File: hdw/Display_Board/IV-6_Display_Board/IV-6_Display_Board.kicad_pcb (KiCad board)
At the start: 4 copper layers, 200 x 50 mm, 236 parts, among them J3001 DSP_IO_Connector, Q1101 PMSTA06, Q1102 BC856W, Q1103 PMSTA06, Q1104 BC856W, Q1105 PMSTA06, Q1106 BC856W, Q1107 PMSTA06, Q1108 BC856W, Q201 PMSTA06, Q202 PMSTA06, Q203 BC856W, Q204 BC856W, Q205 PMSTA06, Q206 PMSTA06, Q207 BC856W, Q208 BC856W, Q209 PMSTA06, Q210 PMSTA06, Q211 BC856W, Q212 BC856W, Q213 PMSTA06, Q214 PMSTA06, Q215 BC856W, Q216 BC856W, Q301 PMSTA06, Q302 PMSTA06, Q303 BC856W, Q304 BC856W, Q305 PMSTA06, Q306 PMSTA06, Q307 BC856W, Q308 BC856W, Q309 PMSTA06, Q310 PMSTA06, Q311 BC856W, Q312 BC856W, SW601 Cap_Touch, SW602 Cap_Touch, SW801 Cap_Touch, SW802 Cap_Touch, SW901 Cap_Touch, U1001 MCP9804, U1301 DS1683, U1302 LTC4316DD, U501 TCA9555RGER, U601 TLV71333PDBV, U602 TLV71333PDBV, U603 AT42QT1010-TSHR, U604 AT42QT1010-TSHR, U605 74LVC1G97, U606 74LVC1G97, U801 TLV71333PDBV, U802 TLV71333PDBV, U803 AT42QT1010-TSHR, U804 AT42QT1010-TSHR, U805 74LVC1G97, U806 74LVC1G97, U901 TLV71333PDBV, U902 AT42QT1010-TSHR, U903 74LVC1G97

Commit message: rotated VFDs
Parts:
- moved Q310 158.3 mm to (368.8, 49.6)
- moved R318 158.3 mm to (368.8, 52.2)
- moved Q301 158.3 mm to (213.2, 49.6)
- moved Q303 158.3 mm to (213.2, 45.0)
- moved Q305 158.3 mm to (235.5, 49.6)
- moved Q306 158.3 mm to (346.6, 49.6)
- moved Q307 158.3 mm to (235.5, 45.0)
- moved Q308 158.3 mm to (346.6, 45.0)
- moved Q309 158.3 mm to (279.9, 49.6)
- moved Q311 158.3 mm to (279.9, 45.0)
- moved Q312 158.3 mm to (368.8, 45.0)
- moved R301 158.3 mm to (213.2, 52.2)
- moved R303 158.3 mm to (216.0, 45.1)
- moved R304 158.3 mm to (213.2, 47.1)
- moved R305 158.3 mm to (304.9, 45.1)
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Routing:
- net Grid_5_VFD: track 8.11 -> 2.99 mm
- net Grid_3_VFD: track 8.23 -> 3.11 mm
- net Grid_0_VFD: track 8.31 -> 3.19 mm
- net Grid_2_VFD: track 8.34 -> 3.22 mm
- net Grid_1_VFD: track 8.38 -> 3.26 mm
- net Grid_4_VFD: track 8.37 -> 3.25 mm
- net GND: vias 79 -> 71

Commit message: Added IV-1 colon tubes
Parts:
- added VFD1101: IV-1, Custom Footprints Library:IV-1, F.Cu at (100.8, 82.3)
- added VFD1102: IV-1, Custom Footprints Library:IV-1, F.Cu at (167.4, 82.3)
- VFD401, VFD402, VFD403, VFD404, VFD405, VFD406: footprint VFD:IV-6 -> Custom Footprints Library:IV-6
- moved R313 166.5 mm to (184.6, 68.7), turned to 0 degrees
- moved R321 166.5 mm to (206.9, 68.7), turned to 0 degrees
- moved R305 166.4 mm to (140.2, 68.7), turned to 0 degrees
- moved R319 166.4 mm to (118.0, 68.7), turned to 0 degrees
- moved R311 166.4 mm to (73.5, 68.8), turned to 0 degrees
- moved R303 166.4 mm to (51.3, 68.8), turned to 0 degrees
- moved Q308 164.1 mm to (184.6, 71.5), turned to 270 degrees
- moved Q312 164.1 mm to (206.8, 71.5), turned to 270 degrees
- moved Q304 164.1 mm to (140.1, 71.5), turned to 270 degrees
- moved Q311 164.1 mm to (117.9, 71.5), turned to 270 degrees
- moved Q307 164.1 mm to (73.5, 71.5), turned to 270 degrees
- moved Q303 164.1 mm to (51.2, 71.5), turned to 270 degrees
- moved R314 161.7 mm to (186.7, 71.5), turned to 270 degrees
- moved R322 161.7 mm to (208.9, 71.5), turned to 270 degrees
- moved R306 161.7 mm to (142.2, 71.5), turned to 270 degrees
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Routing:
- net Net-(R1301-Pad2): track 12.3 -> 3.37 mm
- net Net-(R1302-Pad2): track 11.9 -> 3.37 mm

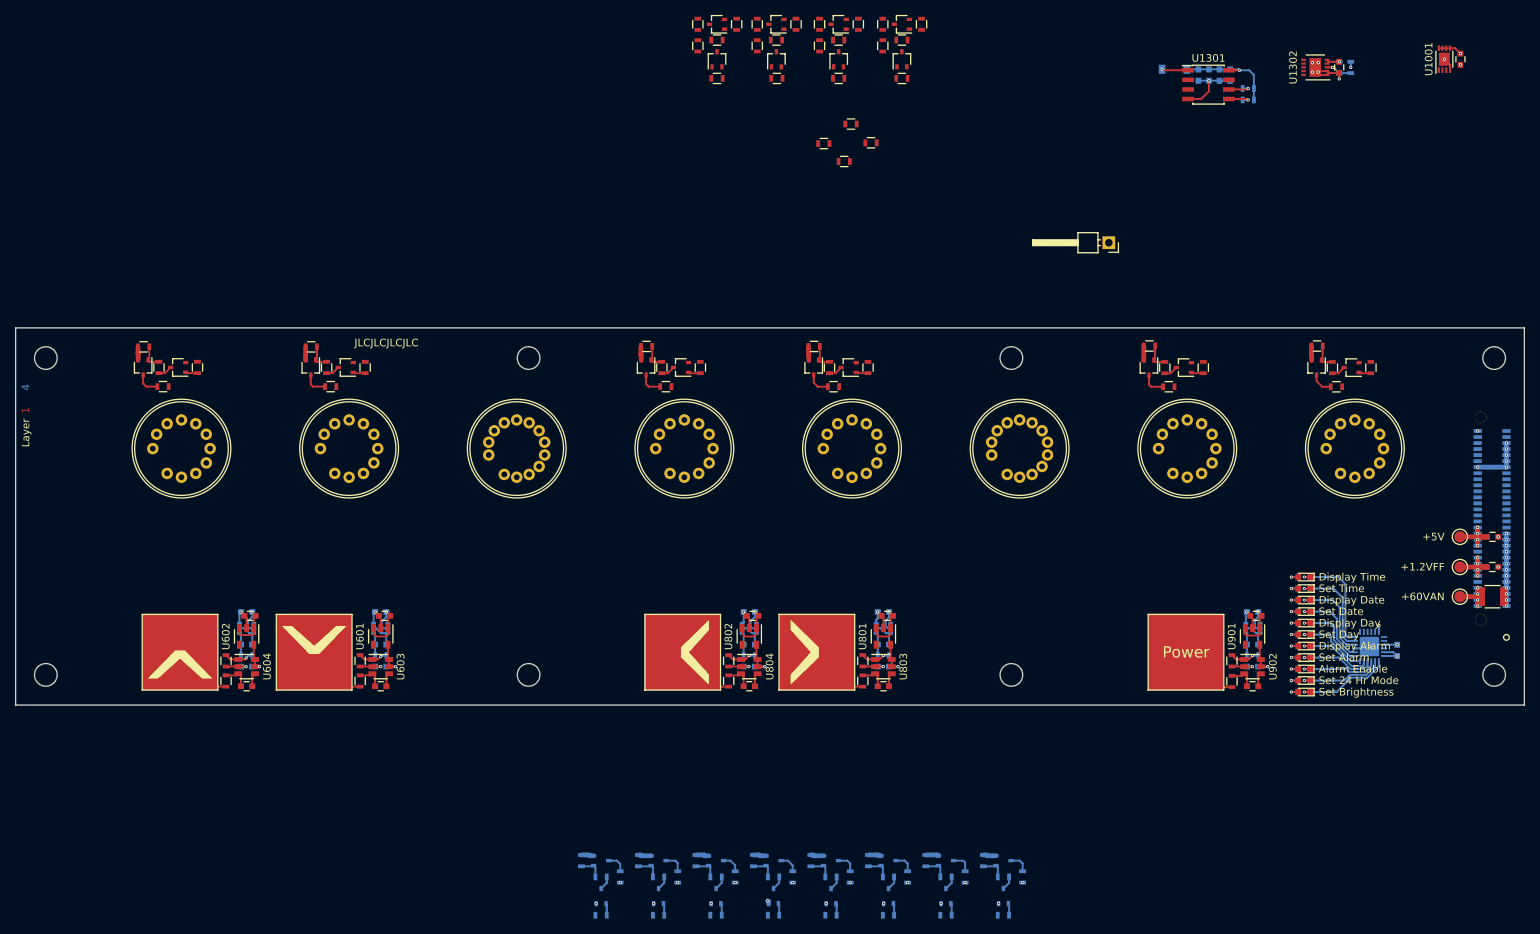
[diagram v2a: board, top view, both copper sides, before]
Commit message: some display board routing, arrangment
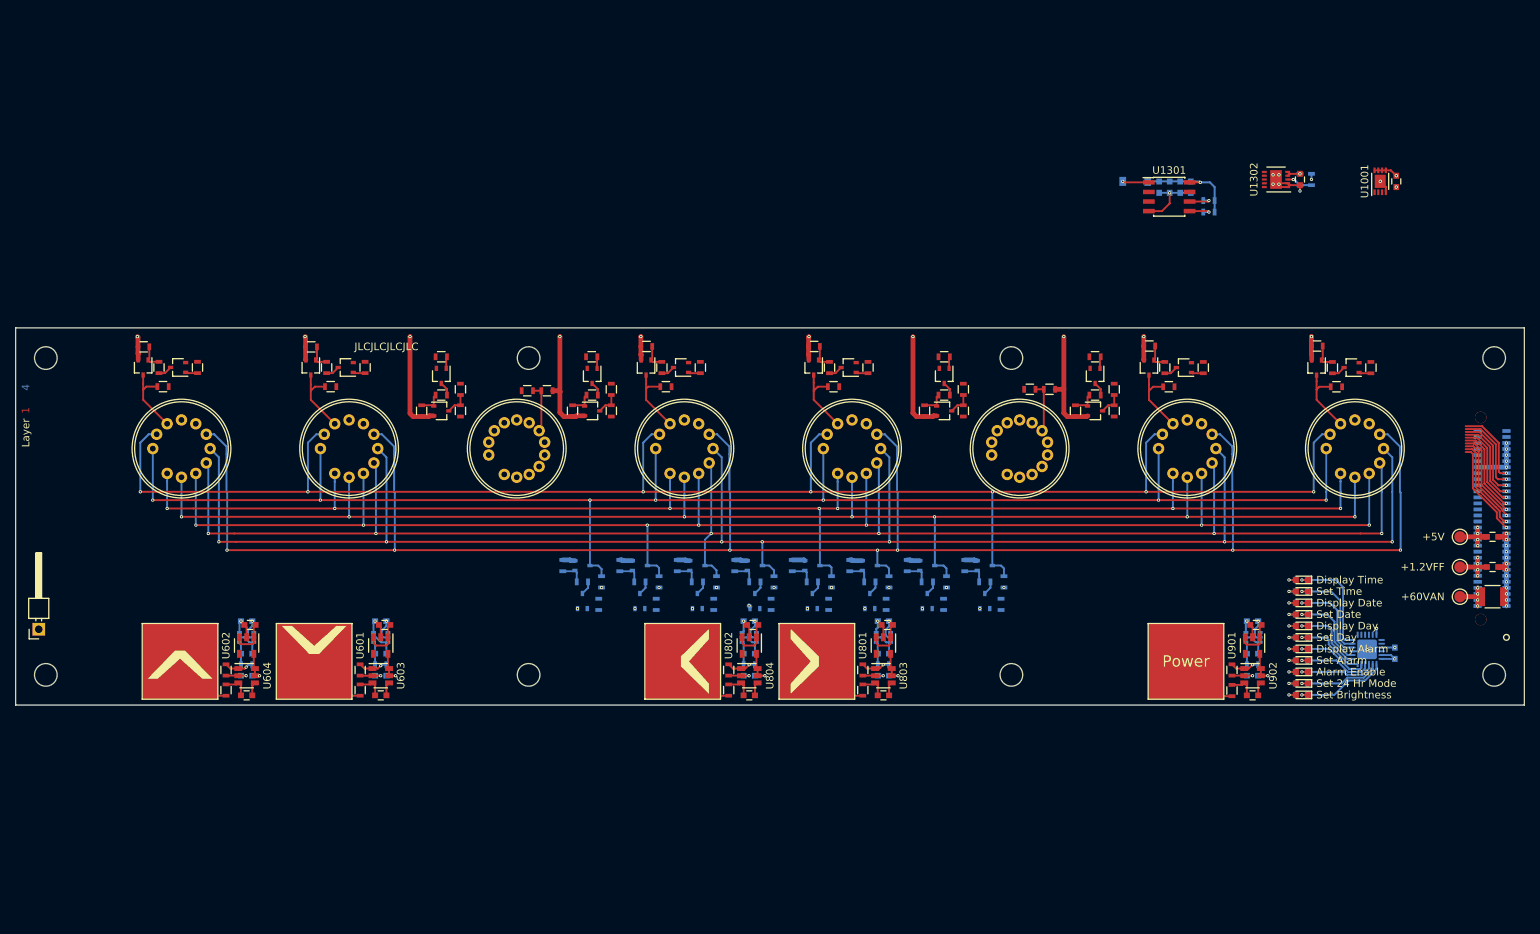
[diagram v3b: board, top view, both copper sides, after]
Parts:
- moved TP704 150.8 mm to (37.4, 106.2), turned to 90 degrees
- moved R1102 66.1 mm to (88.2, 77.3), turned to 90 degrees
- moved Q1102 62.9 mm to (90.8, 77.3), turned to 0 degrees
- moved R1105 60.1 mm to (93.3, 77.3), turned to 90 degrees
- moved R1124 59.7 mm to (180.0, 77.3), turned to 90 degrees
- moved R1103 59.6 mm to (90.8, 75.2), turned to 0 degrees
- moved R1109 59.2 mm to (108.2, 77.3), turned to 90 degrees
- moved Q1108 57.3 mm to (177.4, 77.3), turned to 0 degrees
- moved Q1104 56.8 mm to (110.8, 77.3), turned to 0 degrees
- moved Q1101 55.7 mm to (90.8, 72.6), turned to 270 degrees
- moved R1104 55.4 mm to (93.3, 74.4), turned to 90 degrees
- moved R1121 55.2 mm to (174.8, 77.3), turned to 90 degrees
- moved R1123 54.9 mm to (180.0, 74.4), turned to 90 degrees
- moved R1112 54.8 mm to (113.3, 77.3), turned to 90 degrees
- moved R1119 54.7 mm to (160.0, 77.3), turned to 90 degrees
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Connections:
- VFD1101 pad 1: +1.2VFF -> GND
- VFD1101 pad 8: GND -> +1.2VFF
- VFD1102 pad 1: +1.2VFF -> GND
- VFD1102 pad 8: GND -> +1.2VFF
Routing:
- net +60VAN: track 34.3 -> 318.8 mm, vias 4 -> 14
- net Anode_D_VFD: track 2.73 -> 263.0 mm, vias 0 -> 7
- net Anode_E_VFD: track 2.58 -> 238.3 mm, vias 0 -> 7
- net +1.2VFF: track 11.1 -> 232.7 mm
- net Anode_C_VFD: track 2.73 -> 222.9 mm, vias 0 -> 7
- net Anode_F_VFD: track 2.58 -> 219.5 mm, vias 0 -> 6
- net Anode_DP_VFD: track 2.69 -> 207.9 mm, vias 0 -> 7
- net Anode_G_VFD: track 2.76 -> 204.8 mm, vias 0 -> 7
- net Anode_A_VFD: track 2.73 -> 196.2 mm, vias 0 -> 7
- net Anode_B_VFD: track 2.80 -> 193.9 mm, vias 0 -> 7
- net Colon_3_DSP: track 0.00 -> 12.7 mm, vias 0 -> 1
- net Colon_2_DSP: track 0.00 -> 12.5 mm, vias 0 -> 1
- net Colon_1_DSP: track 0.00 -> 12.0 mm, vias 0 -> 1
- net Colon_0_DSP: track 0.00 -> 11.7 mm, vias 0 -> 1
- net Grid_5_DSP: track 0.00 -> 11.5 mm, vias 0 -> 1
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
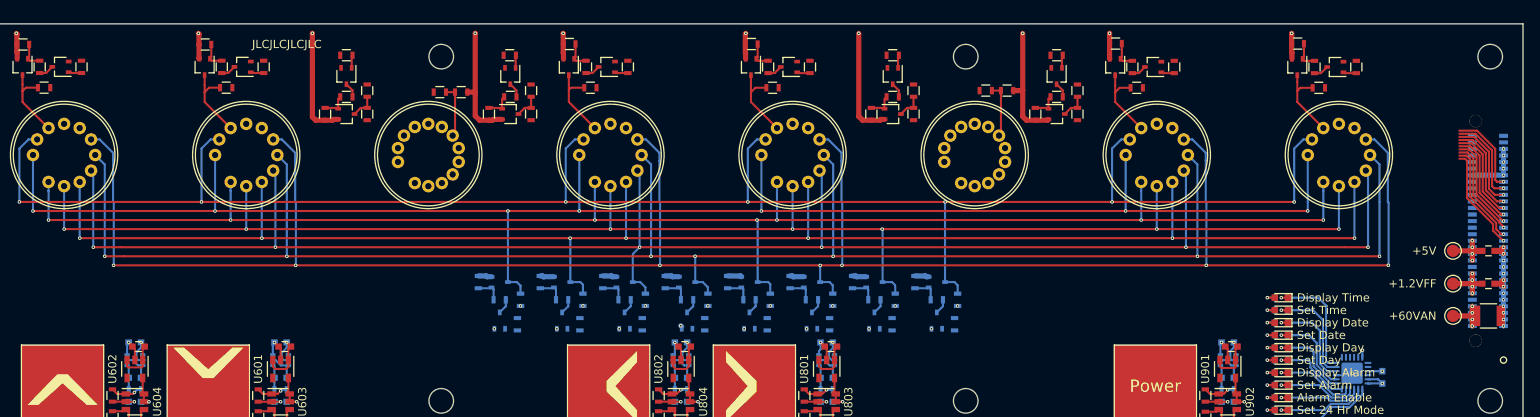
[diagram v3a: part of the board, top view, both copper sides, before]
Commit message: Routed grad and anode drive signals
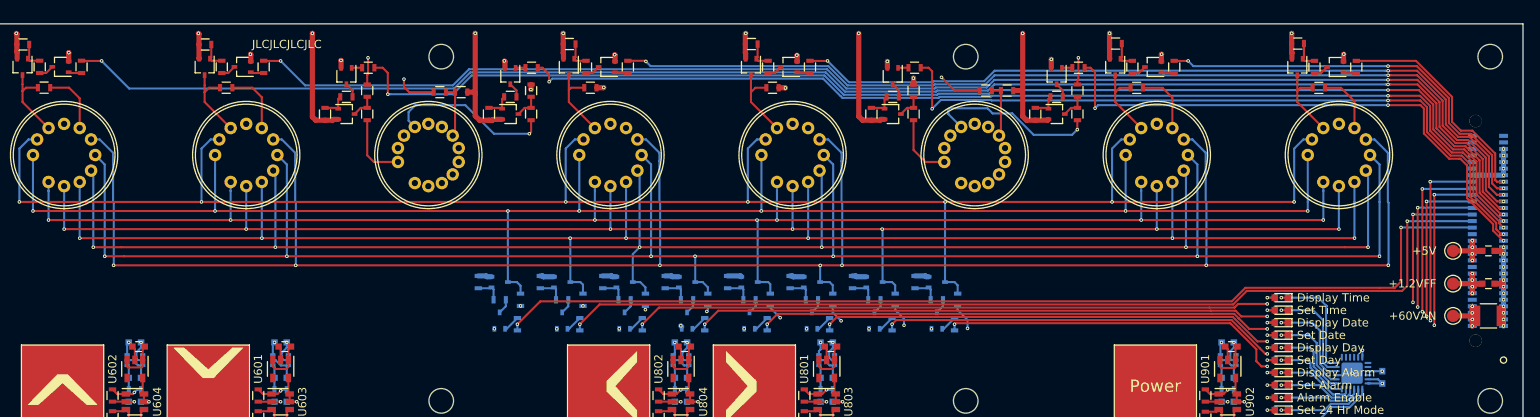
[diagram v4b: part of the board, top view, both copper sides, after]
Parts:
- moved R1101 3.07 mm to (93.4, 71.6), turned to 180 degrees
- moved R1108 3.07 mm to (113.4, 71.6), turned to 180 degrees
- moved R1115 3.07 mm to (160.1, 71.6), turned to 180 degrees
- moved R1120 3.07 mm to (180.1, 71.6), turned to 180 degrees
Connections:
- Q303 pad 3: Grid_0_VFD -> Grid_5_VFD
- Q304 pad 3: Grid_3_VFD -> Grid_2_VFD
- Q307 pad 3: Grid_1_VFD -> Grid_4_VFD
- Q308 pad 3: Grid_4_VFD -> Grid_1_VFD
- Q311 pad 3: Grid_2_VFD -> Grid_3_VFD
- Q312 pad 3: Grid_5_VFD -> Grid_0_VFD
- R301 pad 1: Grid_0_DSP -> Grid_5_DSP
- R302 pad 1: Grid_3_DSP -> Grid_2_DSP
- R307 pad 1: Grid_0_VFD -> Grid_5_VFD
- R308 pad 1: Grid_3_VFD -> Grid_2_VFD
- R309 pad 1: Grid_1_DSP -> Grid_4_DSP
- R310 pad 1: Grid_4_DSP -> Grid_1_DSP
- R315 pad 1: Grid_1_VFD -> Grid_4_VFD
- R316 pad 1: Grid_4_VFD -> Grid_1_VFD
- R317 pad 1: Grid_2_DSP -> Grid_3_DSP
- R318 pad 1: Grid_5_DSP -> Grid_0_DSP
- R323 pad 1: Grid_2_VFD -> Grid_3_VFD
- R324 pad 1: Grid_5_VFD -> Grid_0_VFD
- VFD401 pad 9: Grid_0_VFD -> Grid_5_VFD
- VFD402 pad 9: Grid_3_VFD -> Grid_2_VFD
- VFD403 pad 9: Grid_1_VFD -> Grid_4_VFD
- VFD404 pad 9: Grid_4_VFD -> Grid_1_VFD
- VFD405 pad 9: Grid_2_VFD -> Grid_3_VFD
- VFD406 pad 9: Grid_5_VFD -> Grid_0_VFD
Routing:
- net Grid_5_DSP: track 11.5 -> 187.8 mm, vias 1 -> 3
- net Grid_4_DSP: track 11.3 -> 165.4 mm, vias 1 -> 3
- net Colon_0_DSP: track 11.7 -> 153.5 mm, vias 1 -> 3
- net Anode_DP_DSP: track 0.00 -> 126.0 mm, vias 0 -> 2
- net Anode_G_DSP: track 0.00 -> 119.5 mm, vias 0 -> 2
- net Colon_1_DSP: track 12.0 -> 131.2 mm, vias 1 -> 3
- net Anode_F_DSP: track 0.00 -> 113.9 mm, vias 0 -> 4
- net Anode_E_DSP: track 0.00 -> 108.0 mm, vias 0 -> 4
- net Grid_3_DSP: track 11.2 -> 119.1 mm, vias 1 -> 3
- net Anode_B_DSP: track 0.00 -> 104.0 mm, vias 0 -> 4
- net Anode_D_DSP: track 0.00 -> 96.1 mm, vias 0 -> 4
- net Anode_A_DSP: track 0.00 -> 92.2 mm, vias 0 -> 4
- net Grid_2_DSP: track 11.0 -> 96.5 mm, vias 1 -> 3
- net Anode_C_DSP: track 0.00 -> 85.1 mm, vias 0 -> 4
- net Colon_2_DSP: track 12.5 -> 87.7 mm, vias 1 -> 3
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
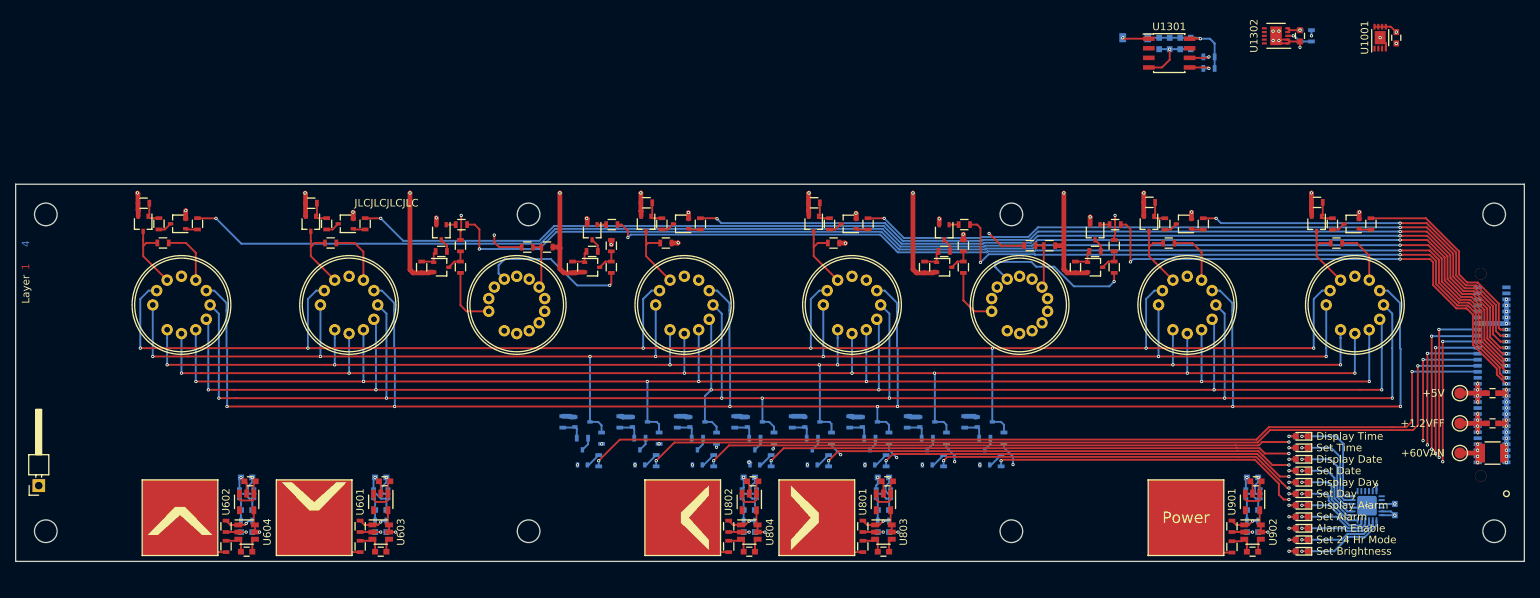
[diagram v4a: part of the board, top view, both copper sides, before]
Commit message: Finished display board layout first pass
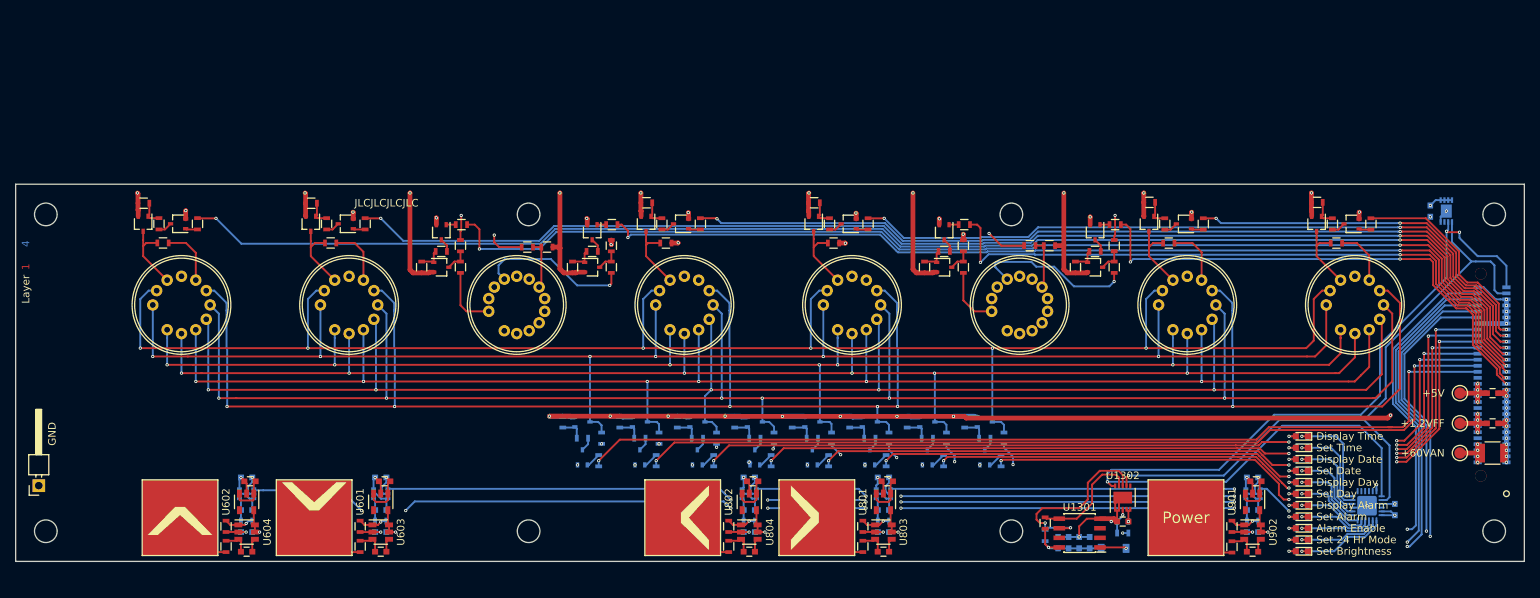
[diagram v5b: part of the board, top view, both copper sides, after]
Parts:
- C1001, U1001: moved to B.Cu
- R1301: moved to F.Cu
- moved R1303 70.5 mm to (181.1, 112.5), turned to 0 degrees
- moved C1305 68.5 mm to (181.1, 111.0), turned to 180 degrees
- moved R1304 68.5 mm to (181.1, 111.0), turned to 180 degrees
- moved C1304 68.5 mm to (172.5, 113.8), turned to 90 degrees
- moved C1301 67.8 mm to (173.9, 113.8), turned to 90 degrees
- moved D1301 67.8 mm to (179.9, 114.6), turned to 0 degrees
- moved C1302 67.2 mm to (175.3, 113.8), turned to 90 degrees
- moved R1302 67.1 mm to (170.8, 112.8), turned to 90 degrees
- moved C1303 66.8 mm to (176.7, 113.8), turned to 90 degrees
- moved U1301 64.7 mm to (175.4, 112.5), turned to 180 degrees
- moved U1302 64.5 mm to (181.1, 107.8), turned to 90 degrees
- moved R1301 64.1 mm to (170.8, 111.2), turned to 90 degrees
- moved U1001 24.6 mm to (224.0, 69.8)
- moved C1001 23.4 mm to (221.9, 69.8)
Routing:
- net Cap_Touch_Up_DSP: track 0.00 -> 202.2 mm, vias 0 -> 8
- net Cap_Touch_Down_DSP: track 0.00 -> 181.4 mm, vias 0 -> 6
- net +60VAN: track 318.8 -> 454.6 mm, vias 14 -> 23
- net Cap_Touch_Left_DSP: track 0.00 -> 130.7 mm, vias 0 -> 4
- net I2C_DSP_SCL: track 0.00 -> 129.7 mm, vias 0 -> 3
- net Cap_Touch_Right_DSP: track 0.00 -> 111.8 mm, vias 0 -> 2
- net I2C_DSP_SDA: track 0.00 -> 90.1 mm, vias 0 -> 1
- net Cap_Touch_Power_DSP: track 0.00 -> 62.0 mm, vias 0 -> 2
- net Net-(R1302-Pad2): track 3.37 -> 24.8 mm, vias 1 -> 2
- net Net-(R1301-Pad2): track 3.37 -> 15.0 mm, vias 1 -> 0
- net GND: track 184.8 -> 194.9 mm, vias 85 -> 81
- net Anode_C_DSP: track 85.1 -> 82.5 mm
- net Anode_A_DSP: track 92.2 -> 89.8 mm
- net Anode_D_DSP: track 96.1 -> 94.1 mm
- net Net-(C1301-Pad1): track 13.9 -> 12.2 mm
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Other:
- board text added: "GND"
